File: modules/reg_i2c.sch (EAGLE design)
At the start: 11 parts, among them U1 P82B715D

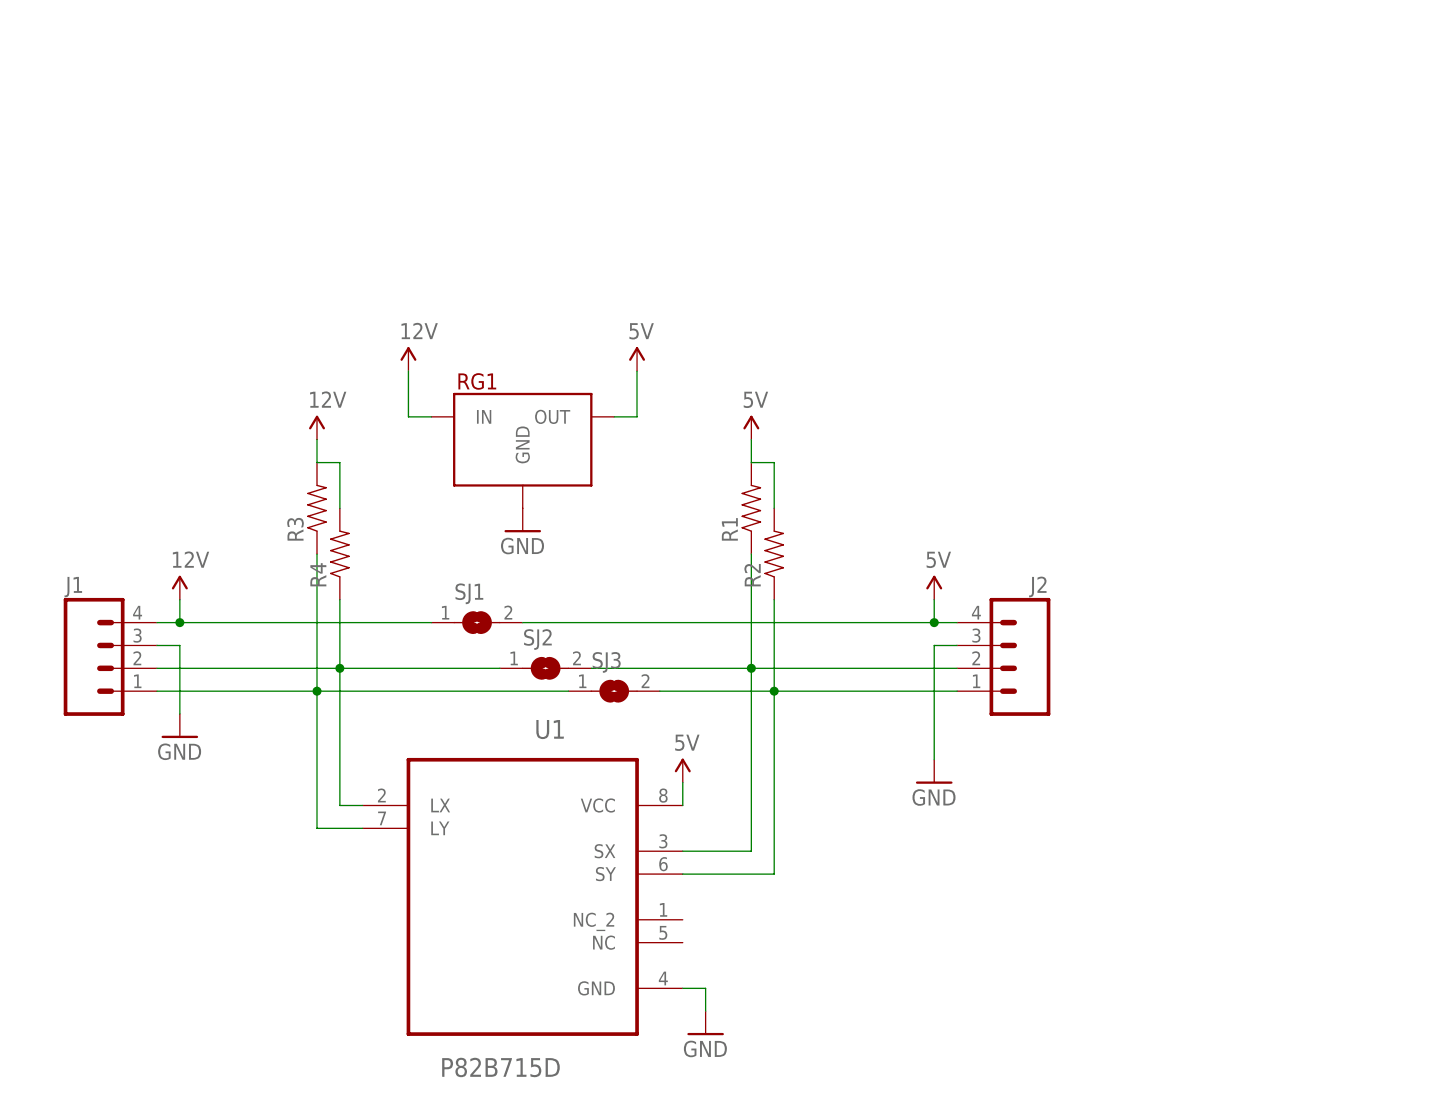
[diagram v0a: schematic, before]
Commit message: V1.0 initial design complete of Regulator board
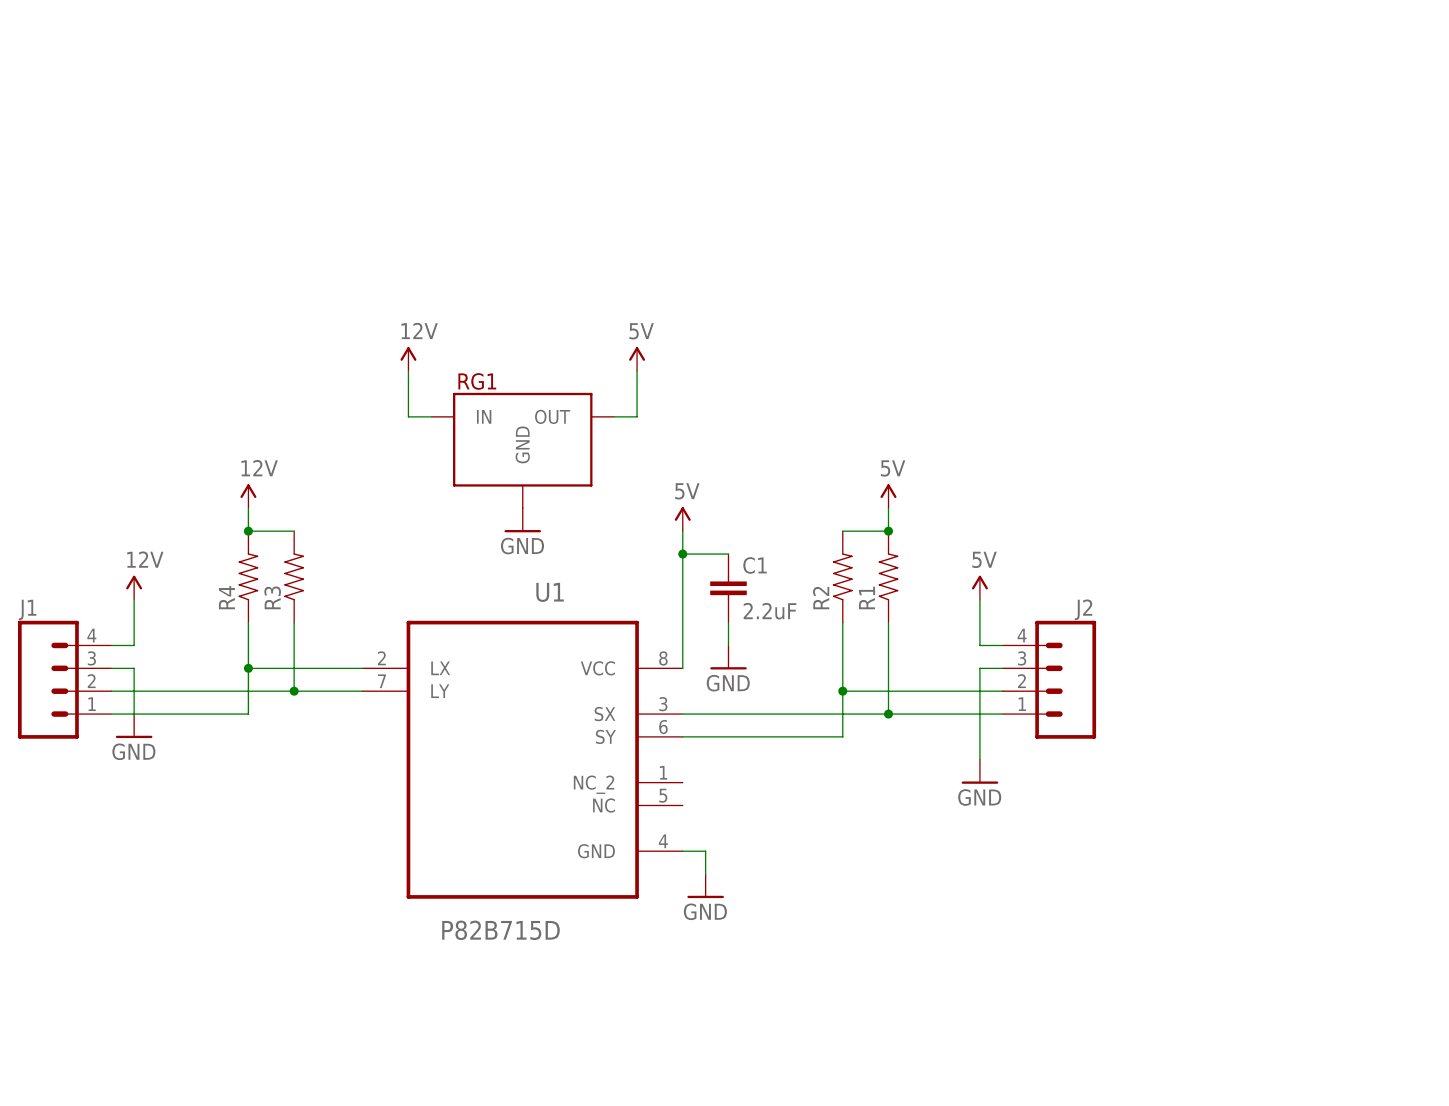
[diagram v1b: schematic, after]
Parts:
- removed SJ1, SJ2, SJ3: (no value), jumper:SJ
- added C1: 2.2uF, SparkFun-Capacitors:2.2UF-10V-20%(0603)
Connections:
- removed net N$3: J2.2, R1.1, SJ2.2, U1.SX
- removed net N$4: J2.1, R2.1, SJ3.2, U1.SY
- new net N$6: J1.2, R3.1, U1.LY
- new net N$7: J1.1, R4.1, U1.LX
- net 12V: no longer SJ1.1
- net 5V: now also C1.1; no longer SJ1.2
- net GND: now also C1.2
- net N$1: now also J2.1, R1.1, U1.SX; no longer J1.2, R4.1, SJ2.1, U1.LX
- net N$2: now also J2.2, R2.1, U1.SY; no longer J1.1, R3.1, SJ3.1, U1.LY
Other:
- moved on the sheet: J1, J2, R1, R2, R3, R4, U1

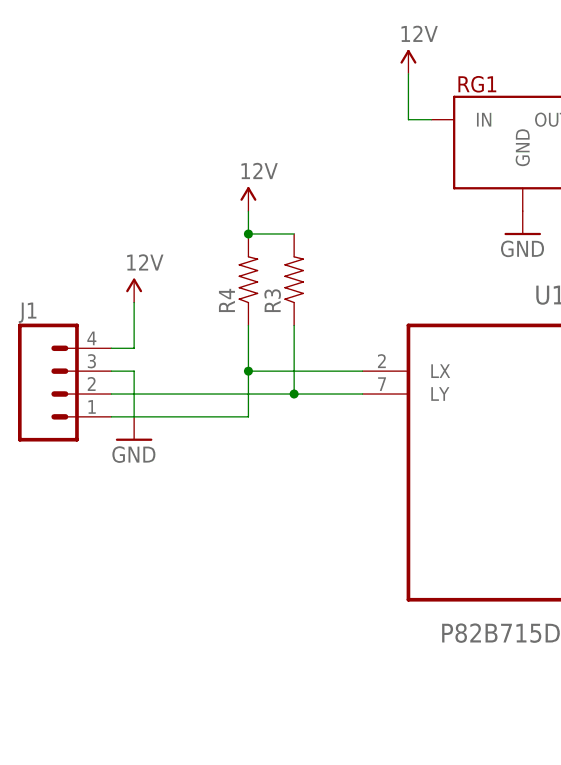
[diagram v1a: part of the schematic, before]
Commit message: Updates to v1 of reg_i2c. New ext_i2c
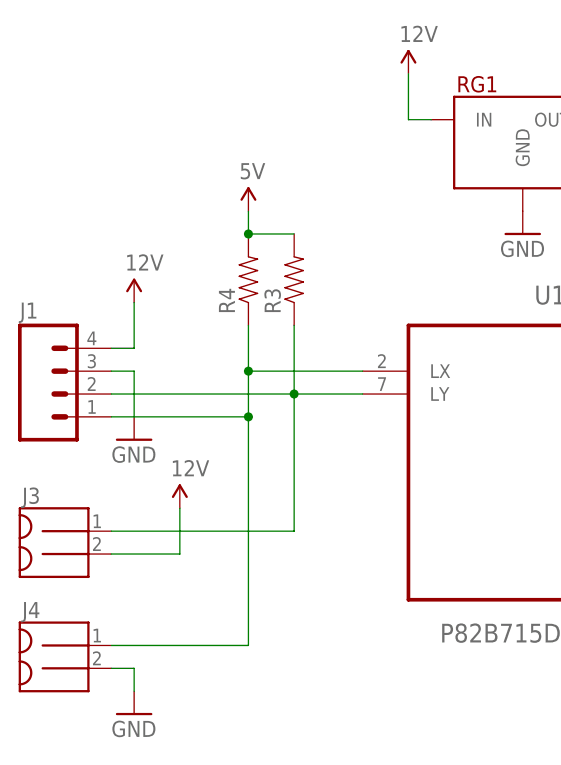
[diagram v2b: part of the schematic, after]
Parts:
- added J3, J4: MOLEX_MINILITE_TRAP_2, Puffin:MOLEX_MINILITE_TRAP_2
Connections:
- net 12V: now also J3.2; no longer R3.2, R4.2
- net 5V: now also R3.2, R4.2
- net GND: now also J4.2
- net N$6: now also J3.1
- net N$7: now also J4.1
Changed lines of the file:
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@@
 <part name="R3" library="SparkFun-Resistors" deviceset="RESISTOR" device="0805-RES"/>
 <part name="R4" library="SparkFun-Resistors" deviceset="RESISTOR" device="0805-RES"/>
-<part name="SUPPLY5" library="SparkFun-Aesthetics" deviceset="12V" device=""/>
 <part name="SUPPLY6" library="SparkFun-Aesthetics" deviceset="5V" device=""/>
 <part name="SUPPLY7" library="SparkFun-Aesthetics" deviceset="5V" device=""/>
 <part name="C1" library="SparkFun-Capacitors" deviceset="2.2UF-10V-20%(0603)" device="" value="2.2uF"/>
 <part name="GND5" library="SparkFun-Aesthetics" deviceset="GND" device=""/>
+<part name="J3" library="Puffin" deviceset="MOLEX_MINILITE_TRAP_2" device=""/>
+<part name="J4" library="Puffin" deviceset="MOLEX_MINILITE_TRAP_2" device=""/>
+<part name="SUPPLY8" library="SparkFun-Aesthetics" deviceset="12V" device=""/>
+<part name="GND6" library="SparkFun-Aesthetics" deviceset="GND" device=""/>
+<part name="SUPPLY5" library="SparkFun-Aesthetics" deviceset="5V" device=""/>
 </parts>
 <sheets>
@@
 <instance part="R3" gate="G$1" x="35.56" y="73.66" rot="R90"/>
 <instance part="R4" gate="G$1" x="30.48" y="73.66" rot="R90"/>
-<instance part="SUPPLY5" gate="G$1" x="30.48" y="81.28"/>
 <instance part="SUPPLY6" gate="G$1" x="101.6" y="81.28"/>
 <instance part="SUPPLY7" gate="G$1" x="78.74" y="78.74"/>
 <instance part="C1" gate="G$1" x="83.82" y="71.12"/>
 <instance part="GND5" gate="1" x="83.82" y="63.5"/>
+<instance part="J3" gate="G$1" x="10.16" y="43.18"/>
+<instance part="J4" gate="G$1" x="10.16" y="30.48"/>
+<instance part="SUPPLY8" gate="G$1" x="22.86" y="48.26"/>
+<instance part="GND6" gate="1" x="17.78" y="25.4"/>
+<instance part="SUPPLY5" gate="G$1" x="30.48" y="81.28"/>
 </instances>
 <busses>
@@
 <wire x1="83.82" y1="68.58" x2="83.82" y2="66.04" width="0.1524" layer="91"/>
 </segment>
+<segment>
+<pinref part="J4" gate="G$1" pin="2"/>
+<pinref part="GND6" gate="1" pin="GND"/>
+<wire x1="15.24" y1="30.48" x2="17.78" y2="30.48" width="0.1524" layer="91"/>
+<wire x1="17.78" y1="30.48" x2="17.78" y2="27.94" width="0.1524" layer="91"/>
+</segment>
 </net>
 <net name="12V" class="0">
@@
 </segment>
 <segment>
-<pinref part="R3" gate="G$1" pin="2"/>
-<wire x1="35.56" y1="78.74" x2="30.48" y2="78.74" width="0.1524" layer="91"/>
-<pinref part="SUPPLY5" gate="G$1" pin="12V"/>
-<pinref part="R4" gate="G$1" pin="2"/>
-<junction x="30.48" y="78.74"/>
-<wire x1="30.48" y1="78.74" x2="30.48" y2="81.28" width="0.1524" layer="91"/>
+<pinref part="J3" gate="G$1" pin="2"/>
+<pinref part="SUPPLY8" gate="G$1" pin="12V"/>
+<wire x1="15.24" y1="43.18" x2="22.86" y2="43.18" width="0.1524" layer="91"/>
+<wire x1="22.86" y1="43.18" x2="22.86" y2="48.26" width="0.1524" layer="91"/>
 </segment>
 </net>
@@
 <junction x="101.6" y="78.74"/>
 </segment>
+<segment>
+<pinref part="R3" gate="G$1" pin="2"/>
+<wire x1="35.56" y1="78.74" x2="30.48" y2="78.74" width="0.1524" layer="91"/>
+<pinref part="R4" gate="G$1" pin="2"/>
+<junction x="30.48" y="78.74"/>
+<wire x1="30.48" y1="78.74" x2="30.48" y2="81.28" width="0.1524" layer="91"/>
+<pinref part="SUPPLY5" gate="G$1" pin="5V"/>
+</segment>
 </net>
 <net name="N$6" class="0">
@@
 <wire x1="15.24" y1="60.96" x2="35.56" y2="60.96" width="0.1524" layer="91"/>
 <junction x="35.56" y="60.96"/>
+<pinref part="J3" gate="G$1" pin="1"/>
+<wire x1="15.24" y1="45.72" x2="35.56" y2="45.72" width="0.1524" layer="91"/>
+<wire x1="35.56" y1="45.72" x2="35.56" y2="60.96" width="0.1524" layer="91"/>
 </segment>
 </net>
@@
 <wire x1="43.18" y1="63.5" x2="30.48" y2="63.5" width="0.1524" layer="91"/>
 <junction x="30.48" y="63.5"/>
+<pinref part="J4" gate="G$1" pin="1"/>
+<wire x1="15.24" y1="33.02" x2="30.48" y2="33.02" width="0.1524" layer="91"/>
+<wire x1="30.48" y1="33.02" x2="30.48" y2="58.42" width="0.1524" layer="91"/>
+<junction x="30.48" y="58.42"/>
 </segment>
 </net>

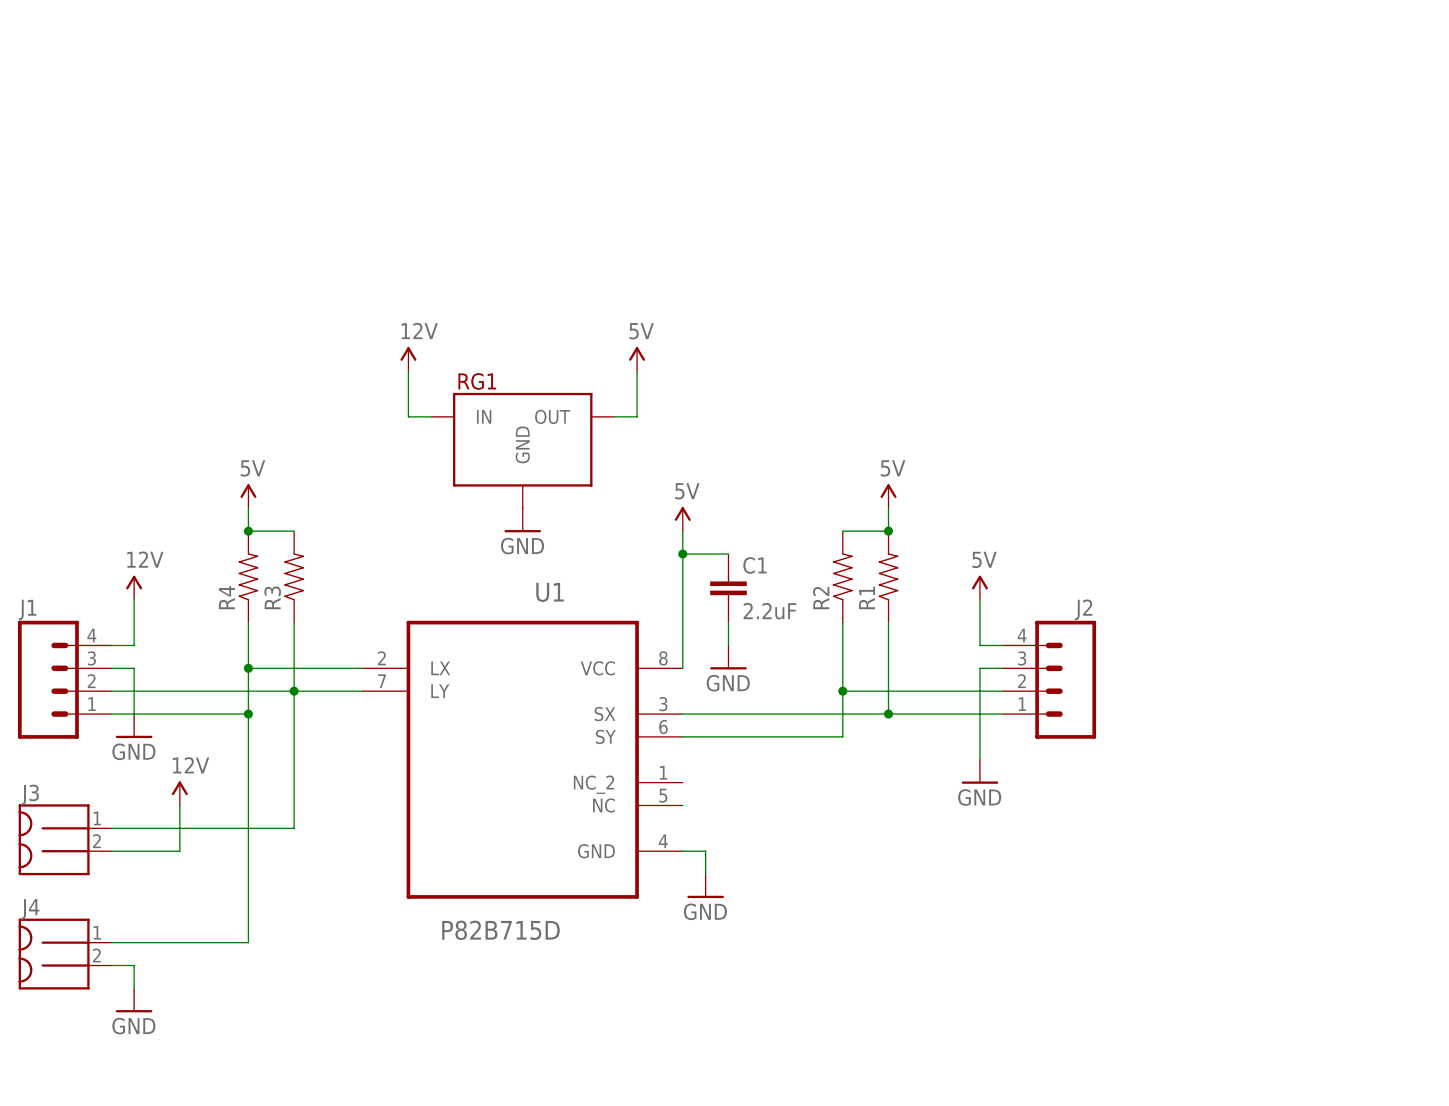
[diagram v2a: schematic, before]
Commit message: Change reg_i2c to use a 2x8 header
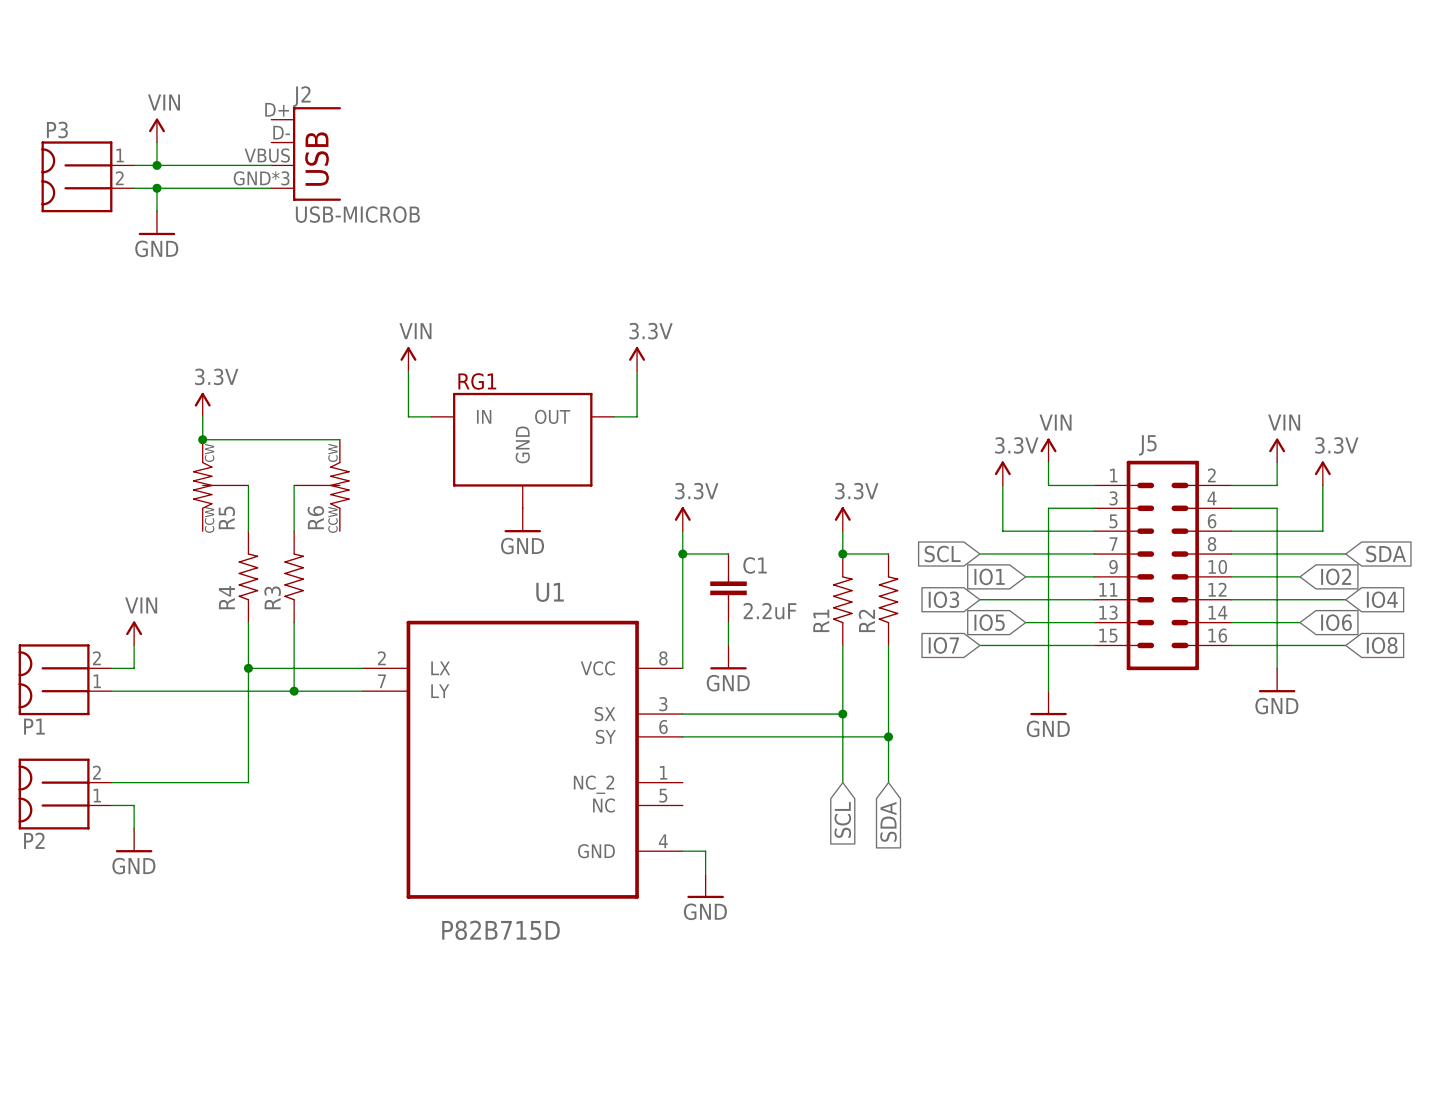
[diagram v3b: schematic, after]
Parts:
- removed J1: (no value), SparkFun-Connectors:M04PTH
- removed J3, J4: MOLEX_MINILITE_TRAP_2, Puffin:MOLEX_MINILITE_TRAP_2
- added J5: (no value), SparkFun-Connectors:M08X2
- added P1, P2, P3: MOLEX_MINILITE_TRAP_2, Puffin:MOLEX_MINILITE_TRAP_2
- added R5, R6: (no value), Puffin:POT_3MM
- J2: value (none) -> USB-MICROB; device SparkFun-Connectors:M04PTH -> SparkFun-Connectors:USB-MICROB
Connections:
- removed net 12V: J1.4, J3.2, RG1.IN
- removed net 5V: C1.1, J2.4, R1.2, R2.2, R3.2, R4.2, RG1.OUT, U1.VCC
- removed net N$1: J2.1, R1.1, U1.SX
- removed net N$2: J2.2, R2.1, U1.SY
- new net 3.3V: C1.1, J5.5, J5.6, R1.2, R2.2, R5.3, R6.3, RG1.OUT, U1.VCC
- new net IO1: J5.9
- new net IO2: J5.10
- new net IO3: J5.11
- new net IO4: J5.12
- new net IO5: J5.13
- new net IO6: J5.14
- new net IO7: J5.15
- new net IO8: J5.16
- new net N$3: R3.2, R6.2
- new net N$4: R4.2, R5.2
- new net SCL: J5.7, R1.1, U1.SX
- new net SDA: J5.8, R2.1, U1.SY
- new net VIN: J2.VBUS, J5.1, J5.2, P1.2, P3.1, RG1.IN
- net GND: now also J2.GND, J5.3, J5.4, P2.1, P3.2; no longer J1.3, J2.3, J4.2
- net N$6: now also P1.1; no longer J1.2, J3.1
- net N$7: now also P2.2; no longer J1.1, J4.1
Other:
- moved on the sheet: R1, R2

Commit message: Gate 4, and misc updates
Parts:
- removed J2: USB-MICROB, SparkFun-Connectors:USB-MICROB
- added U$1: USB_MICRO, Puffin:USB_MICRO
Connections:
- net IO2 renamed IO15
- net IO3 renamed IO17
- net IO5 renamed IO27
- net IO7 renamed IO22
- net IO8 renamed IO23
- removed net IO1: J5.9
- removed net IO6: J5.14
- new net IO14: J5.8
- new net IO18: J5.12
- net 3.3V: now also J5.1; no longer J5.5, J5.6
- net GND: now also J5.14, J5.6, J5.9, U$1.5; no longer J2.GND, J5.3, J5.4
- net IO4: now also J5.7; no longer J5.12
- net N$3: now also R4.2; no longer R3.2
- net N$4: now also R3.2; no longer R4.2
- net N$6: now also P2.2, R4.1; no longer P1.1, R3.1
- net N$7: now also P1.1, R3.1; no longer P2.2, R4.1
- net SCL: now also J5.5; no longer J5.7
- net SDA: now also J5.3; no longer J5.8
- net VIN: now also J5.4, U$1.1; no longer J2.VBUS, J5.1
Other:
- moved on the sheet: J5, P1, R3, R4
